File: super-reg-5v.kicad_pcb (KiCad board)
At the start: 2 copper layers, 85 x 35 mm, 45 parts, among them Q1 2SA1015, Q2 D44H11, U1 LM317T, U2 AD825, U3 AD825, X1 AC_IN, X2 DC_OUT

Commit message: update components
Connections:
- Q1 pad 3: Net-(LED1-Pad1) -> Net-(Q1-Pad3)
- R3 pad 1: Net-(LED1-Pad1) -> Net-(Q1-Pad3)
- U2 pad 1: (no net) -> Net-(U2-Pad1)
- U2 pad 5: (no net) -> Net-(U2-Pad5)
- U2 pad 8: (no net) -> Net-(U2-Pad8)
- U3 pad 1: (no net) -> Net-(U3-Pad1)
- U3 pad 5: (no net) -> Net-(U3-Pad5)
- U3 pad 8: (no net) -> Net-(U3-Pad8)
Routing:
- net Net-(Q1-Pad3): track 0.00 -> 9.59 mm
- net Net-(LED1-Pad1): track 11.4 -> 1.80 mm
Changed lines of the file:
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@@
-(kicad_pcb (version 4) (host pcbnew 4.0.4-stable)
+(kicad_pcb (version 4) (host pcbnew 4.0.6)
   (general
-    (links 78)
+    (links 77)
     (no_connects 0)
-    (area 103.422857 69.206 207.473143 112.631)
+    (area 112.924999 73.924999 198.075001 109.075001)
     (thickness 1.6)
     (drawings 14)
@@
     (zones 0)
     (modules 45)
-    (nets 18)
+    (nets 25)
   )
   (page A4)
@@
   )
   (setup
-    (last_trace_width 2)
+    (last_trace_width 0.25)
     (user_trace_width 0.3)
     (user_trace_width 0.5)
@@
   (net 16 /OPAMP_P)
   (net 17 /OPAMP_N)
+  (net 18 "Net-(Q1-Pad3)")
+  (net 19 "Net-(U2-Pad1)")
+  (net 20 "Net-(U2-Pad5)")
+  (net 21 "Net-(U2-Pad8)")
+  (net 22 "Net-(U3-Pad1)")
+  (net 23 "Net-(U3-Pad5)")
+  (net 24 "Net-(U3-Pad8)")
   (net_class Default "This is the default net class."
     (clearance 0.25)
@@
     (add_net "Net-(LED1-Pad1)")
     (add_net "Net-(Q1-Pad1)")
+    (add_net "Net-(Q1-Pad3)")
     (add_net "Net-(R1-Pad2)")
     (add_net "Net-(R6-Pad1)")
+    (add_net "Net-(U2-Pad1)")
+    (add_net "Net-(U2-Pad5)")
+    (add_net "Net-(U2-Pad8)")
+    (add_net "Net-(U3-Pad1)")
+    (add_net "Net-(U3-Pad5)")
+    (add_net "Net-(U3-Pad8)")
   )
   (module Mounting_Holes:MountingHole_3.2mm_M3 (layer F.Cu)
@@
       (net 14 "Net-(C5-Pad1)"))
     (pad 3 thru_hole circle (at 5.08 0 90) (size 1.524 1.524) (drill 0.8) (layers *.Cu *.Mask F.SilkS)
-      (net 10 "Net-(LED1-Pad1)"))
+      (net 18 "Net-(Q1-Pad3)"))
     (pad 1 thru_hole circle (at 0 0 90) (size 1.524 1.524) (drill 0.8) (layers *.Cu *.Mask F.SilkS)
       (net 11 "Net-(Q1-Pad1)"))
@@
     (fp_line (start 0.135 9.915) (end 7.485 9.915) (layer F.SilkS) (width 0.15))
     (fp_line (start 0.135 -1.025) (end -0.8 -1.025) (layer F.SilkS) (width 0.15))
-    (pad 1 thru_hole oval (at 0 0 90) (size 1.6 1.6) (drill 0.8) (layers *.Cu *.Mask F.SilkS))
+    (pad 1 thru_hole oval (at 0 0 90) (size 1.6 1.6) (drill 0.8) (layers *.Cu *.Mask F.SilkS)
+      (net 19 "Net-(U2-Pad1)"))
     (pad 2 thru_hole oval (at 0 2.54 90) (size 1.6 1.6) (drill 0.8) (layers *.Cu *.Mask F.SilkS)
       (net 17 /OPAMP_N))
@@
     (pad 4 thru_hole oval (at 0 7.62 90) (size 1.6 1.6) (drill 0.8) (layers *.Cu *.Mask F.SilkS)
       (net 2 GND))
-    (pad 5 thru_hole oval (at 7.62 7.62 90) (size 1.6 1.6) (drill 0.8) (layers *.Cu *.Mask F.SilkS))
+    (pad 5 thru_hole oval (at 7.62 7.62 90) (size 1.6 1.6) (drill 0.8) (layers *.Cu *.Mask F.SilkS)
+      (net 20 "Net-(U2-Pad5)"))
     (pad 6 thru_hole oval (at 7.62 5.08 90) (size 1.6 1.6) (drill 0.8) (layers *.Cu *.Mask F.SilkS)
       (net 13 "Net-(R6-Pad1)"))
     (pad 7 thru_hole oval (at 7.62 2.54 90) (size 1.6 1.6) (drill 0.8) (layers *.Cu *.Mask F.SilkS)
       (net 15 /OPAMP_PW))
-    (pad 8 thru_hole oval (at 7.62 0 90) (size 1.6 1.6) (drill 0.8) (layers *.Cu *.Mask F.SilkS))
+    (pad 8 thru_hole oval (at 7.62 0 90) (size 1.6 1.6) (drill 0.8) (layers *.Cu *.Mask F.SilkS)
+      (net 21 "Net-(U2-Pad8)"))
     (model Housings_DIP.3dshapes/DIP-8_W7.62mm.wrl
       (at (xyz 0 0 0))
@@
     (fp_line (start -2.075 2.575) (end 2.075 2.575) (layer F.SilkS) (width 0.15))
     (fp_line (start -2.075 -2.43) (end -3.475 -2.43) (layer F.SilkS) (width 0.15))
-    (pad 1 smd rect (at -2.7 -1.905 180) (size 1.55 0.6) (layers F.Cu F.Paste F.Mask))
+    (pad 1 smd rect (at -2.7 -1.905 180) (size 1.55 0.6) (layers F.Cu F.Paste F.Mask)
+      (net 22 "Net-(U3-Pad1)"))
     (pad 2 smd rect (at -2.7 -0.635 180) (size 1.55 0.6) (layers F.Cu F.Paste F.Mask)
       (net 17 /OPAMP_N))
@@
     (pad 4 smd rect (at -2.7 1.905 180) (size 1.55 0.6) (layers F.Cu F.Paste F.Mask)
       (net 2 GND))
-    (pad 5 smd rect (at 2.7 1.905 180) (size 1.55 0.6) (layers F.Cu F.Paste F.Mask))
+    (pad 5 smd rect (at 2.7 1.905 180) (size 1.55 0.6) (layers F.Cu F.Paste F.Mask)
+      (net 23 "Net-(U3-Pad5)"))
     (pad 6 smd rect (at 2.7 0.635 180) (size 1.55 0.6) (layers F.Cu F.Paste F.Mask)
       (net 13 "Net-(R6-Pad1)"))
     (pad 7 smd rect (at 2.7 -0.635 180) (size 1.55 0.6) (layers F.Cu F.Paste F.Mask)
       (net 15 /OPAMP_PW))
-    (pad 8 smd rect (at 2.7 -1.905 180) (size 1.55 0.6) (layers F.Cu F.Paste F.Mask))
+    (pad 8 smd rect (at 2.7 -1.905 180) (size 1.55 0.6) (layers F.Cu F.Paste F.Mask)
+      (net 24 "Net-(U3-Pad8)"))
     (model Housings_SOIC.3dshapes/SOIC-8_3.9x4.9mm_Pitch1.27mm.wrl
       (at (xyz 0 0 0))
@@
     (fp_line (start -0.5 -0.675) (end 0.5 -0.675) (layer F.SilkS) (width 0.15))
     (pad 1 smd rect (at -1.1 0) (size 1.2 0.9) (layers F.Cu F.Paste F.Mask)
-      (net 10 "Net-(LED1-Pad1)"))
+      (net 18 "Net-(Q1-Pad3)"))
     (pad 2 smd rect (at 1.1 0) (size 1.2 0.9) (layers F.Cu F.Paste F.Mask)
       (net 2 GND))
@@
   (segment (start 173.99 100.33) (end 174.752 101.092) (width 0.5) (layer B.Cu) (net 9))
   (segment (start 179.07 99.822) (end 179.07 99.314) (width 0.5) (layer B.Cu) (net 9))
-  (segment (start 153.332 94.742) (end 153.332 93.896) (width 0.8) (layer F.Cu) (net 10))
-  (segment (start 153.332 93.896) (end 151.638 92.202) (width 0.8) (layer F.Cu) (net 10))
-  (segment (start 151.638 92.202) (end 151.638 85.852) (width 0.8) (layer B.Cu) (net 10))
   (segment (start 151.638 85.852) (end 150.368 84.582) (width 0.8) (layer B.Cu) (net 10))
   (segment (start 146.558 92.202) (end 146.558 87.71) (width 0.8) (layer B.Cu) (net 11))
@@
   (segment (start 167.64 94.615) (end 167.64 96.698) (width 0.5) (layer F.Cu) (net 17))
   (segment (start 167.64 96.698) (end 166.548 97.79) (width 0.5) (layer F.Cu) (net 17))
+  (segment (start 153.332 94.742) (end 153.332 93.896) (width 0.8) (layer F.Cu) (net 18))
+  (segment (start 153.332 93.896) (end 151.638 92.202) (width 0.8) (layer F.Cu) (net 18))
+  (segment (start 151.638 92.202) (end 151.638 85.852) (width 0.8) (layer B.Cu) (net 18))
 )

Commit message: fix library error
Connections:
- Q1 pad 3: Net-(Q1-Pad3) -> Net-(LED1-Pad1)
- R3 pad 1: Net-(Q1-Pad3) -> Net-(LED1-Pad1)
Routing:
- net Net-(Q1-Pad3): track 9.59 -> 0.00 mm
- net Net-(LED1-Pad1): track 1.80 -> 11.4 mm
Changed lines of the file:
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@@
 (kicad_pcb (version 4) (host pcbnew 4.0.6)
   (general
-    (links 77)
+    (links 78)
     (no_connects 0)
     (area 112.924999 73.924999 198.075001 109.075001)
@@
     (zones 0)
     (modules 45)
-    (nets 25)
+    (nets 24)
   )
   (page A4)
@@
   (net 16 /OPAMP_P)
   (net 17 /OPAMP_N)
-  (net 18 "Net-(Q1-Pad3)")
-  (net 19 "Net-(U2-Pad1)")
-  (net 20 "Net-(U2-Pad5)")
-  (net 21 "Net-(U2-Pad8)")
-  (net 22 "Net-(U3-Pad1)")
-  (net 23 "Net-(U3-Pad5)")
-  (net 24 "Net-(U3-Pad8)")
+  (net 18 "Net-(U2-Pad1)")
+  (net 19 "Net-(U2-Pad5)")
+  (net 20 "Net-(U2-Pad8)")
+  (net 21 "Net-(U3-Pad1)")
+  (net 22 "Net-(U3-Pad5)")
+  (net 23 "Net-(U3-Pad8)")
   (net_class Default "This is the default net class."
     (clearance 0.25)
@@
     (add_net "Net-(LED1-Pad1)")
     (add_net "Net-(Q1-Pad1)")
-    (add_net "Net-(Q1-Pad3)")
     (add_net "Net-(R1-Pad2)")
     (add_net "Net-(R6-Pad1)")
@@
       (net 14 "Net-(C5-Pad1)"))
     (pad 3 thru_hole circle (at 5.08 0 90) (size 1.524 1.524) (drill 0.8) (layers *.Cu *.Mask F.SilkS)
-      (net 18 "Net-(Q1-Pad3)"))
+      (net 10 "Net-(LED1-Pad1)"))
     (pad 1 thru_hole circle (at 0 0 90) (size 1.524 1.524) (drill 0.8) (layers *.Cu *.Mask F.SilkS)
       (net 11 "Net-(Q1-Pad1)"))
@@
     (fp_line (start 0.135 -1.025) (end -0.8 -1.025) (layer F.SilkS) (width 0.15))
     (pad 1 thru_hole oval (at 0 0 90) (size 1.6 1.6) (drill 0.8) (layers *.Cu *.Mask F.SilkS)
-      (net 19 "Net-(U2-Pad1)"))
+      (net 18 "Net-(U2-Pad1)"))
     (pad 2 thru_hole oval (at 0 2.54 90) (size 1.6 1.6) (drill 0.8) (layers *.Cu *.Mask F.SilkS)
       (net 17 /OPAMP_N))
@@
       (net 2 GND))
     (pad 5 thru_hole oval (at 7.62 7.62 90) (size 1.6 1.6) (drill 0.8) (layers *.Cu *.Mask F.SilkS)
-      (net 20 "Net-(U2-Pad5)"))
+      (net 19 "Net-(U2-Pad5)"))
     (pad 6 thru_hole oval (at 7.62 5.08 90) (size 1.6 1.6) (drill 0.8) (layers *.Cu *.Mask F.SilkS)
       (net 13 "Net-(R6-Pad1)"))
@@
       (net 15 /OPAMP_PW))
     (pad 8 thru_hole oval (at 7.62 0 90) (size 1.6 1.6) (drill 0.8) (layers *.Cu *.Mask F.SilkS)
-      (net 21 "Net-(U2-Pad8)"))
+      (net 20 "Net-(U2-Pad8)"))
     (model Housings_DIP.3dshapes/DIP-8_W7.62mm.wrl
       (at (xyz 0 0 0))
@@
     (fp_line (start -2.075 -2.43) (end -3.475 -2.43) (layer F.SilkS) (width 0.15))
     (pad 1 smd rect (at -2.7 -1.905 180) (size 1.55 0.6) (layers F.Cu F.Paste F.Mask)
-      (net 22 "Net-(U3-Pad1)"))
+      (net 21 "Net-(U3-Pad1)"))
     (pad 2 smd rect (at -2.7 -0.635 180) (size 1.55 0.6) (layers F.Cu F.Paste F.Mask)
       (net 17 /OPAMP_N))
@@
       (net 2 GND))
     (pad 5 smd rect (at 2.7 1.905 180) (size 1.55 0.6) (layers F.Cu F.Paste F.Mask)
-      (net 23 "Net-(U3-Pad5)"))
+      (net 22 "Net-(U3-Pad5)"))
     (pad 6 smd rect (at 2.7 0.635 180) (size 1.55 0.6) (layers F.Cu F.Paste F.Mask)
       (net 13 "Net-(R6-Pad1)"))
@@
       (net 15 /OPAMP_PW))
     (pad 8 smd rect (at 2.7 -1.905 180) (size 1.55 0.6) (layers F.Cu F.Paste F.Mask)
-      (net 24 "Net-(U3-Pad8)"))
+      (net 23 "Net-(U3-Pad8)"))
     (model Housings_SOIC.3dshapes/SOIC-8_3.9x4.9mm_Pitch1.27mm.wrl
       (at (xyz 0 0 0))
@@
     (fp_line (start -0.5 -0.675) (end 0.5 -0.675) (layer F.SilkS) (width 0.15))
     (pad 1 smd rect (at -1.1 0) (size 1.2 0.9) (layers F.Cu F.Paste F.Mask)
-      (net 18 "Net-(Q1-Pad3)"))
+      (net 10 "Net-(LED1-Pad1)"))
     (pad 2 smd rect (at 1.1 0) (size 1.2 0.9) (layers F.Cu F.Paste F.Mask)
       (net 2 GND))
@@
   (segment (start 179.07 99.822) (end 179.07 99.314) (width 0.5) (layer B.Cu) (net 9))
   (segment (start 151.638 85.852) (end 150.368 84.582) (width 0.8) (layer B.Cu) (net 10))
+  (segment (start 153.332 94.742) (end 153.332 93.896) (width 0.8) (layer F.Cu) (net 10))
+  (segment (start 153.332 93.896) (end 151.638 92.202) (width 0.8) (layer F.Cu) (net 10))
+  (segment (start 151.638 92.202) (end 151.638 85.852) (width 0.8) (layer B.Cu) (net 10))
   (segment (start 146.558 92.202) (end 146.558 87.71) (width 0.8) (layer B.Cu) (net 11))
   (segment (start 146.558 87.71) (end 146.812 87.456) (width 0.8) (layer B.Cu) (net 11))
@@
   (segment (start 167.64 94.615) (end 167.64 96.698) (width 0.5) (layer F.Cu) (net 17))
   (segment (start 167.64 96.698) (end 166.548 97.79) (width 0.5) (layer F.Cu) (net 17))
-  (segment (start 153.332 94.742) (end 153.332 93.896) (width 0.8) (layer F.Cu) (net 18))
-  (segment (start 153.332 93.896) (end 151.638 92.202) (width 0.8) (layer F.Cu) (net 18))
-  (segment (start 151.638 92.202) (end 151.638 85.852) (width 0.8) (layer B.Cu) (net 18))
 )

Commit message: update footprints
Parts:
- C11, C8: footprint Capacitors_ThroughHole:C_Radial_D8_L13_P3.8 -> Capacitors_ThroughHole:CP_Radial_D8.0mm_P3.80mm
- C3, C5, C6, C9: footprint Capacitors_ThroughHole:C_Radial_D6.3_L11.2_P2.5 -> Capacitors_ThroughHole:CP_Radial_D6.3mm_P2.50mm
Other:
- board text added: "2017-05-18"
- board text removed: "2017-01-10"

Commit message: minor fix
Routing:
- net Net-(R1-Pad2): track 22.0 -> 21.1 mm
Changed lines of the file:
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@@
     (links 78)
     (no_connects 0)
-    (area 112.924999 73.924999 198.075001 109.075001)
+    (area 103.422857 69.206 207.473143 112.631)
     (thickness 1.6)
     (drawings 14)
@@
     (35 F.Paste user)
     (36 B.SilkS user hide)
-    (37 F.SilkS user)
+    (37 F.SilkS user hide)
     (38 B.Mask user)
     (39 F.Mask user)
@@
       (psa4output false)
       (plotreference true)
-      (plotvalue false)
+      (plotvalue true)
       (plotinvisibletext false)
       (padsonsilk false)
@@
   (segment (start 185.166 77.316) (end 185.166 78.232) (width 2.5) (layer B.Cu) (net 6))
   (segment (start 167.132 82.296) (end 167.132 81.28) (width 0.3) (layer B.Cu) (net 6))
-  (segment (start 167.132 81.28) (end 166.497 80.645) (width 0.3) (layer B.Cu) (net 6))
-  (segment (start 166.497 80.645) (end 156.337 80.645) (width 0.3) (layer B.Cu) (net 6))
-  (segment (start 156.337 80.645) (end 155.786 81.196) (width 0.3) (layer B.Cu) (net 6))
+  (segment (start 167.132 81.28) (end 166.624 80.772) (width 0.3) (layer B.Cu) (net 6))
+  (segment (start 166.624 80.772) (end 156.21 80.772) (width 0.3) (layer B.Cu) (net 6))
+  (segment (start 156.21 80.772) (end 155.786 81.196) (width 0.3) (layer B.Cu) (net 6))
   (segment (start 155.786 81.196) (end 155.786 82.804) (width 0.3) (layer B.Cu) (net 6))
   (segment (start 168.91 76.2) (end 168.91 80.01) (width 0.8) (layer B.Cu) (net 6))
@@
   (segment (start 144.78 82.677) (end 143.68 81.577) (width 0.5) (layer B.Cu) (net 12))
   (via (at 144.78 82.677) (size 0.8) (drill 0.4) (layers F.Cu B.Cu) (net 12))
-  (segment (start 144.78 84.455) (end 144.78 82.677) (width 0.5) (layer F.Cu) (net 12))
-  (segment (start 147.32 86.995) (end 144.78 84.455) (width 0.5) (layer F.Cu) (net 12))
-  (segment (start 151.384 86.995) (end 147.32 86.995) (width 0.5) (layer F.Cu) (net 12))
+  (segment (start 144.78 82.55) (end 144.78 82.677) (width 0.5) (layer F.Cu) (net 12))
+  (segment (start 149.225 86.995) (end 144.78 82.55) (width 0.5) (layer F.Cu) (net 12))
+  (segment (start 151.384 86.995) (end 149.225 86.995) (width 0.5) (layer F.Cu) (net 12))
   (segment (start 153.797 84.582) (end 151.384 86.995) (width 0.5) (layer F.Cu) (net 12))
   (via (at 153.797 84.582) (size 0.8) (drill 0.4) (layers F.Cu B.Cu) (net 12))

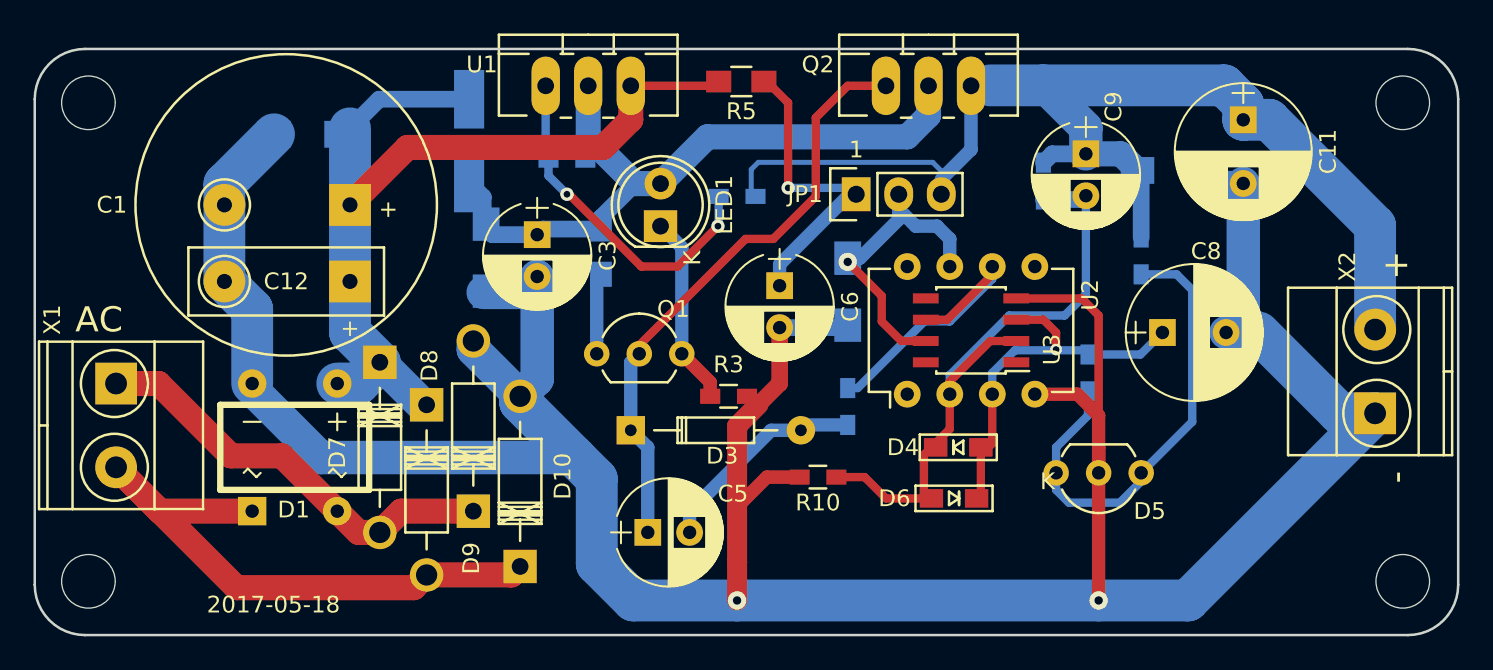
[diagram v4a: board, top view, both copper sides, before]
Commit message: separate sensor input refactor components
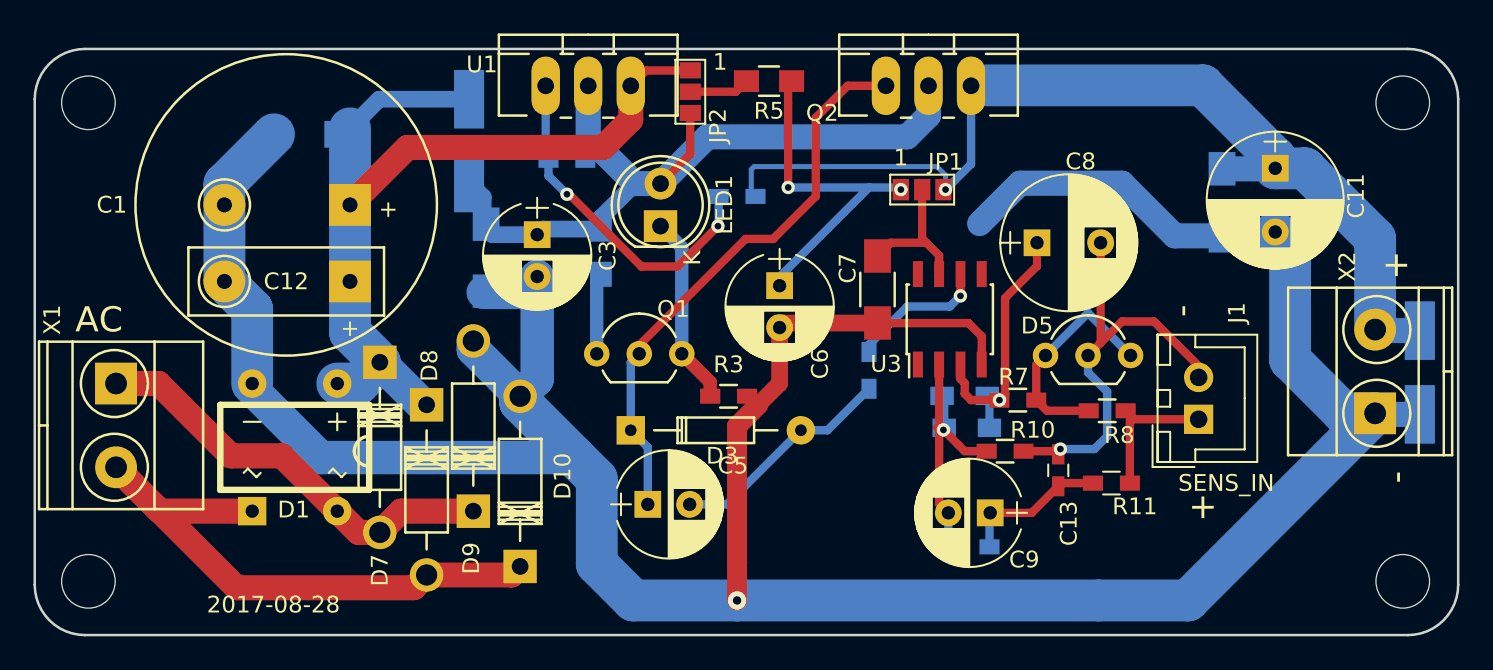
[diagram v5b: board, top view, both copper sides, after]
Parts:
- removed U2: AD825, Housings_DIP:DIP-8_W7.62mm
- added C13: 100p, Capacitors_SMD:C_0603_HandSoldering, F.Cu at (174.1, 99.2)
- added D11: D, Diodes_SMD:D_SMA_Handsoldering, B.Cu at (195.7, 93.3)
- added J1: SENS_IN, Connectors_JST:JST_XH_B02B-XH-A_02x2.50mm_Straight, F.Cu at (182.5, 96.1)
- added JP2: OPAMP_PWR_1, Connect:GS3, F.Cu at (152.1, 76.6)
- added R11: 100, Resistors_SMD:R_0603_HandSoldering, F.Cu at (177.3, 99.9)
- C7, R7, R8: moved to F.Cu
- D1: value DB-1S -> DB-1S(SDI2100)
- D2: footprint Diodes_SMD:SMA_Handsoldering -> Diodes_SMD:D_SMA_Handsoldering
- D4, D6: moved to B.Cu
- JP1: value OPAMP_PWR -> OPAMP_PWR_2; footprint Pin_Headers:Pin_Header_Straight_1x03 -> Connect:GS3
- Q1: value 2SA1015 -> 2SA1015GR
- moved R9 22.3 mm to (168.9, 103.7), turned to 180 degrees
- moved C9 22.2 mm to (170.1, 101.7), turned to 180 degrees
- moved R10 11.3 mm to (170.9, 98.0), turned to 0 degrees
- moved R8 9.47 mm to (177.0, 95.6), turned to 0 degrees
- moved C8 9.21 mm to (172.8, 85.6)
- moved D5 9.04 mm to (173.4, 92.3), turned to 0 degrees
- moved D6 6.15 mm to (168.5, 94.7)
- moved R7 4.49 mm to (171.7, 95.0), turned to 180 degrees
- moved JP1 3.95 mm to (166.0, 82.4)
- moved C10 3.59 mm to (183.9, 83.2), turned to 270 degrees
- moved C11 3.47 mm to (187.1, 81.1)
- moved R6 2.50 mm to (162.8, 93.2)
- moved C7 1.78 mm to (163.3, 88.4)
- moved C5 1.68 mm to (149.6, 101.2)
- moved R5 1.65 mm to (156.8, 75.9)
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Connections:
- C8 pad 2: GND -> Net-(C13-Pad1)
- C9 pad 1: Net-(C10-Pad1) -> Net-(C13-Pad2)
- D5 pad 2: GND -> Net-(C13-Pad1)
- R10 pad 2: GND -> Net-(C13-Pad1)
- R5 pad 2: Net-(C1-Pad1) -> Net-(JP2-Pad2)
- R8 pad 2: Net-(C10-Pad1) -> Net-(J1-Pad1)
- R9 pad 1: Net-(C10-Pad1) -> Net-(C13-Pad2)
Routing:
- net Net-(C13-Pad1): track 0.00 -> 26.1 mm, vias 0 -> 1
- net /OPAMP_N: track 38.1 -> 16.9 mm, vias 0 -> 1
- net Net-(D5-Pad1): track 28.7 -> 13.5 mm
- net GND: track 198.5 -> 186.9 mm, vias 2 -> 1
- net Net-(C10-Pad1): track 70.5 -> 60.1 mm, vias 0 -> 1
- net /OPAMP_PW: track 18.7 -> 8.72 mm, vias 1 -> 0
- net Net-(R6-Pad1): track 17.6 -> 8.40 mm, vias 0 -> 1
- net Net-(J1-Pad1): track 0.00 -> 8.99 mm
- net Net-(C13-Pad2): track 0.00 -> 8.93 mm
- net /OPAMP_P: track 22.9 -> 17.2 mm
- net Net-(C3-Pad1): track 43.3 -> 48.2 mm
- net Net-(JP2-Pad2): track 0.00 -> 3.61 mm
- net Net-(C6-Pad1): track 19.2 -> 21.5 mm, vias 1 -> 2
- net Net-(C5-Pad1): track 37.0 -> 35.3 mm
- net Net-(C1-Pad1): track 56.4 -> 55.0 mm
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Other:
- board text added: "2017-08-28"
- board text removed: "2017-05-18"

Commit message: fix track add sensor line silk minor fix
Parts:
- moved D5 0.38 mm to (173.0, 92.3)
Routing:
- net Net-(C13-Pad1): track 26.1 -> 29.8 mm
- net Net-(D5-Pad1): track 13.5 -> 14.3 mm
- net Net-(C10-Pad1): vias 1 -> 2
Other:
- board text added: "*"
- board text added: "OUT"
